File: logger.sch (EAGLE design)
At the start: 55 parts, among them IC1 LTC4412, J1 POWER_JACKPTH, Q1 FDN360P, Q2 FDN360P, U1 FT232RL

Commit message: exposed interfaces, button update, board layout
(1) Exposed SPI, I2C, and UART interfaces
(2) Added 1K resistors to UART to allow switching away from the computer
(3) Updated the buttons to PTH (higher button: RESET), PTH DPDT b/c of
    availability (LOG NOW)
(4) Reworked the board layout to keep the same form factor while adding
    many new screw terminals (and keeping the 3.5 mm spacing)
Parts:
- removed H2: (no value), SparkFun:M04SCREW
- removed S2: Reset, SparkFun:TAC_SWITCHSND
- added JP6: (no value), SparkFun-Connectors:M04SCREW
- added RESET: Reset, SparkFun-Electromechanical:SWITCH-MOMENTARY-2PTH
- added RX_SW: 1Kohm, rcl:R-US_R0603
- added TX_SW: 1K, rcl:R-US_R0603
- COUT: device SmartPrj:C-EUC0603 -> rcl:C-EUC0603
- MANUAL_LOG: device awickert:TL3350'TL3350' -> switch-misc:PVA1
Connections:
- removed net CS-EXT: H3.6
- removed net D7: H1.6, MCU.PD7(AIN1)
- new net D7-CS-EXT: H3.4, MCU.PD7(AIN1)
- new net N$10: TX_SW.1, U1.RXD
- new net N$9: RX_SW.1, U1.TXD
- net +3V3: now also H1.2, H1.4, H3.7; no longer H2.2, H2.4
- net A6: now also H1.1; no longer H2.1
- net A7: now also H1.3; no longer H2.3
- net CLK: now also H3.3; no longer H3.5
- net D3-INT1: now also H1.5; no longer H1.1
- net D5_MANUAL_LOG: now also MANUAL_LOG2.S; no longer MANUAL_LOG.M1
- net D6: now also H1.8; no longer H1.5
- net DI: now also H3.1; no longer H3.3
- net DO: now also H3.2; no longer H3.4
- net GND: now also H1.6, H3.6, MANUAL_LOG1.P, MANUAL_LOG2.P, RESET.1; no longer H1.2, H1.4, H1.7, MANUAL_LOG.COM1, MANUAL_LOG.COM2, S2.1, S2.2
- net INT0: now also MANUAL_LOG1.S; no longer MANUAL_LOG.M2
- net RESET: now also RESET.2; no longer S2.3, S2.4
- net RX-I: now also JP6.1, RX_SW.2; no longer H3.1, U1.TXD
- net SCL: now also JP6.4; no longer H3.8
- net SDA: now also JP6.3; no longer H3.7
- net TX-O: now also JP6.2, TX_SW.2; no longer H3.2, U1.RXD
- net VCC: now also H1.7, H3.5; no longer H1.3, H1.8
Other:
- moved on the sheet: H1, H3

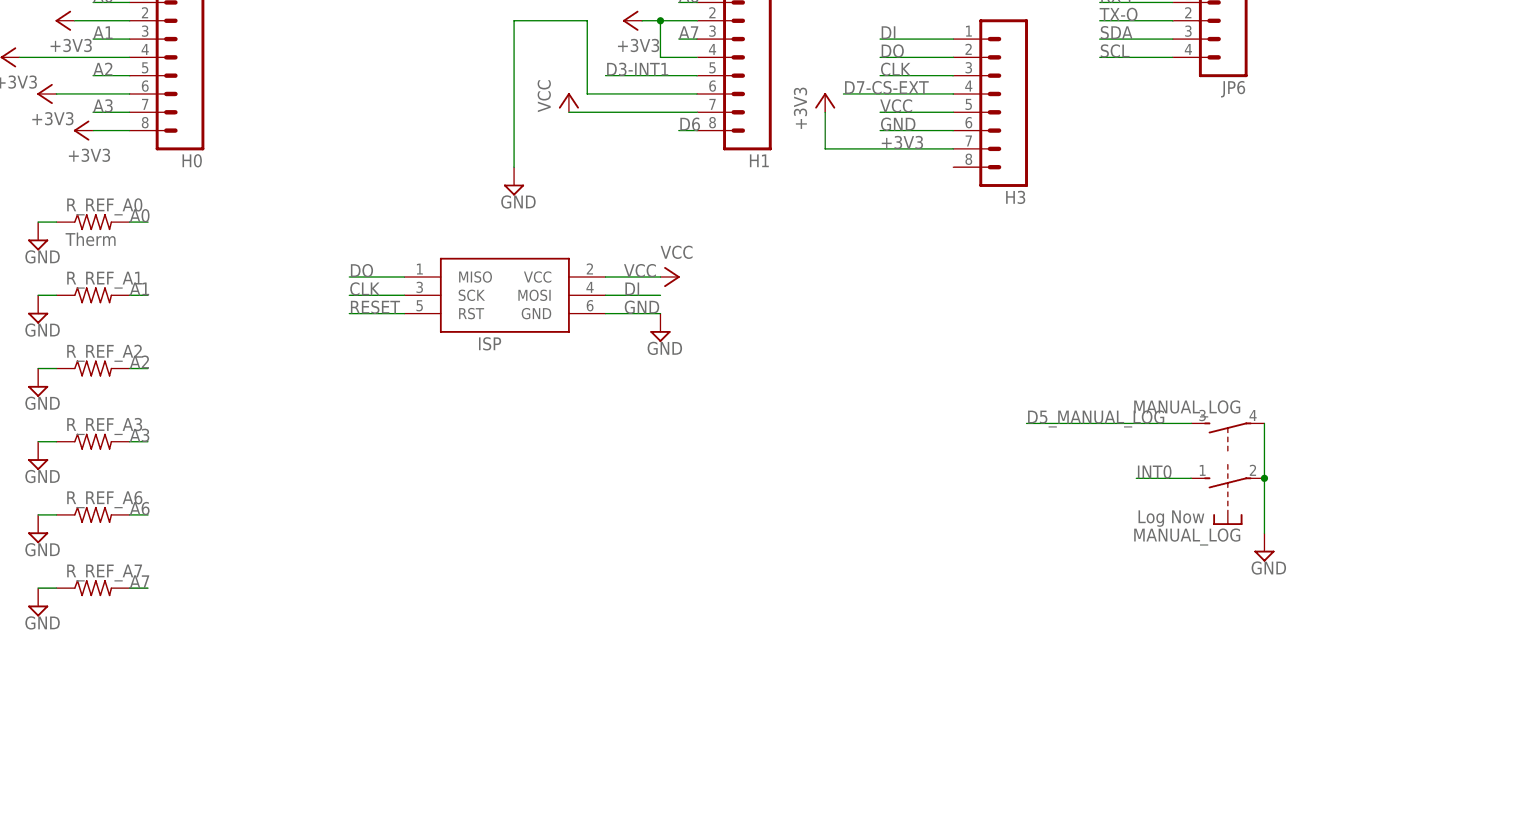
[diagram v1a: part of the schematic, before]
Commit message: 10nF chip caps for analog, following Gerhard Oberforcher
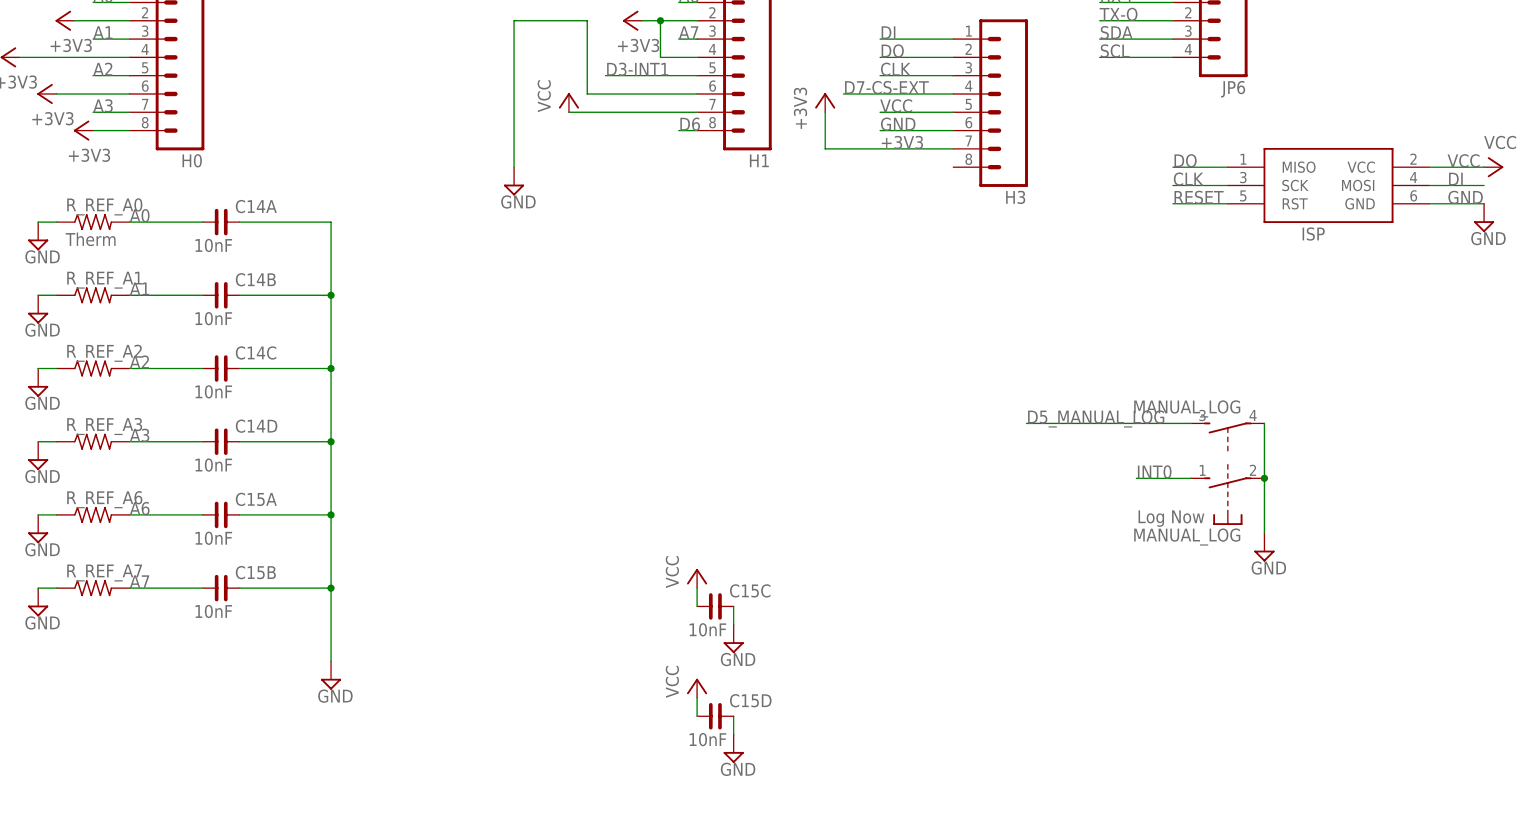
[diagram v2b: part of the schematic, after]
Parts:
- added C14, C15: 10nF, rc-master-smd:CCA_ECJ-0805
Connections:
- net A0: now also C14A.1
- net A1: now also C14B.1
- net A2: now also C14C.1
- net A3: now also C14D.1
- net A6: now also C15A.1
- net A7: now also C15B.1
- net GND: now also C14A.2, C14B.2, C14C.2, C14D.2, C15A.2, C15B.2, C15C.2, C15D.2
- net VCC: now also C15C.1, C15D.1
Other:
- moved on the sheet: ISP
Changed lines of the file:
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@@
 <clearance class="2" value="0.2032"/>
+</class>
+<class number="3" name="usbvcc" width="0.508" drill="0.508">
+<clearance class="3" value="0.1524"/>
+</class>
+<class number="4" name="aref" width="0.4064" drill="0">
 </class>
 </classes>
@@
 <part name="MANUAL_LOG" library="switch-misc" deviceset="PVA1" device="" value="Log Now"/>
 <part name="RESET" library="SparkFun-Electromechanical" deviceset="SWITCH-MOMENTARY-2" device="PTH" value="Reset"/>
+<part name="C14" library="rc-master-smd" deviceset="CCA_" device="ECJ-0805" value="10nF"/>
+<part name="C15" library="rc-master-smd" deviceset="CCA_" device="ECJ-0805" value="10nF"/>
+<part name="SUPPLY27" library="supply2" deviceset="GND" device=""/>
+<part name="SUPPLY37" library="supply2" deviceset="GND" device=""/>
+<part name="SUPPLY38" library="supply2" deviceset="GND" device=""/>
+<part name="P+17" library="supply1" deviceset="VCC" device=""/>
+<part name="P+22" library="supply1" deviceset="VCC" device=""/>
 </parts>
 <sheets>
@@
 <instance part="R_REF_A3" gate="G$1" x="208.28" y="58.42"/>
 <instance part="SUPPLY13" gate="GND" x="185.42" y="200.66"/>
-<instance part="ISP" gate="G$1" x="264.16" y="78.74"/>
-<instance part="P+11" gate="VCC" x="289.56" y="81.28" rot="R270"/>
-<instance part="SUPPLY14" gate="GND" x="287.02" y="73.66"/>
+<instance part="ISP" gate="G$1" x="378.46" y="93.98"/>
+<instance part="P+11" gate="VCC" x="403.86" y="96.52" rot="R270"/>
+<instance part="SUPPLY14" gate="GND" x="401.32" y="88.9"/>
 <instance part="PU1" gate="G$1" x="284.48" y="226.06" rot="R90"/>
 <instance part="PU2" gate="G$1" x="297.18" y="223.52" rot="R90"/>
@@
 <instance part="MANUAL_LOG" gate="2" x="365.76" y="60.96" rot="R90"/>
 <instance part="RESET" gate="G$1" x="88.9" y="149.86" rot="R90"/>
+<instance part="C14" gate="A" x="226.06" y="88.9"/>
+<instance part="C14" gate="B" x="226.06" y="78.74"/>
+<instance part="C14" gate="C" x="226.06" y="68.58"/>
+<instance part="C14" gate="D" x="226.06" y="58.42"/>
+<instance part="C15" gate="A" x="226.06" y="48.26"/>
+<instance part="C15" gate="B" x="226.06" y="38.1"/>
+<instance part="C15" gate="C" x="294.64" y="35.56"/>
+<instance part="C15" gate="D" x="294.64" y="20.32"/>
+<instance part="SUPPLY27" gate="GND" x="241.3" y="25.4"/>
+<instance part="SUPPLY37" gate="GND" x="297.18" y="15.24"/>
+<instance part="SUPPLY38" gate="GND" x="297.18" y="30.48"/>
+<instance part="P+17" gate="VCC" x="292.1" y="40.64"/>
+<instance part="P+22" gate="VCC" x="292.1" y="25.4"/>
 </instances>
 <busses>
@@
 </segment>
 <segment>
-<wire x1="279.4" y1="81.28" x2="287.02" y2="81.28" width="0.1524" layer="91"/>
-<label x="281.94" y="81.28" size="1.778" layer="95"/>
+<wire x1="393.7" y1="96.52" x2="401.32" y2="96.52" width="0.1524" layer="91"/>
+<label x="396.24" y="96.52" size="1.778" layer="95"/>
 <pinref part="ISP" gate="G$1" pin="VCC"/>
 <pinref part="P+11" gate="VCC" pin="VCC"/>
@@
 <pinref part="H3" gate="G$1" pin="5"/>
 </segment>
+<segment>
+<pinref part="C15" gate="C" pin="1"/>
+<wire x1="292.1" y1="35.56" x2="292.1" y2="38.1" width="0.1524" layer="91"/>
+<pinref part="P+17" gate="VCC" pin="VCC"/>
+</segment>
+<segment>
+<pinref part="C15" gate="D" pin="1"/>
+<wire x1="292.1" y1="20.32" x2="292.1" y2="22.86" width="0.1524" layer="91"/>
+<pinref part="P+22" gate="VCC" pin="VCC"/>
+</segment>
 </net>
 <net name="CS-SD" class="0">
@@
 </segment>
 <segment>
-<wire x1="279.4" y1="78.74" x2="287.02" y2="78.74" width="0.1524" layer="91"/>
-<label x="281.94" y="78.74" size="1.778" layer="95"/>
+<wire x1="393.7" y1="93.98" x2="401.32" y2="93.98" width="0.1524" layer="91"/>
+<label x="396.24" y="93.98" size="1.778" layer="95"/>
 <pinref part="ISP" gate="G$1" pin="MOSI"/>
 </segment>
@@
 </segment>
 <segment>
-<wire x1="251.46" y1="81.28" x2="243.84" y2="81.28" width="0.1524" layer="91"/>
-<label x="243.84" y="81.28" size="1.778" layer="95"/>
+<wire x1="365.76" y1="96.52" x2="358.14" y2="96.52" width="0.1524" layer="91"/>
+<label x="358.14" y="96.52" size="1.778" layer="95"/>
 <pinref part="ISP" gate="G$1" pin="MISO"/>
 </segment>
@@
 </segment>
 <segment>
-<wire x1="251.46" y1="78.74" x2="243.84" y2="78.74" width="0.1524" layer="91"/>
-<label x="243.84" y="78.74" size="1.778" layer="95"/>
+<wire x1="365.76" y1="93.98" x2="358.14" y2="93.98" width="0.1524" layer="91"/>
+<label x="358.14" y="93.98" size="1.778" layer="95"/>
 <pinref part="ISP" gate="G$1" pin="SCK"/>
 </segment>
@@
 </segment>
 <segment>
-<wire x1="279.4" y1="76.2" x2="287.02" y2="76.2" width="0.1524" layer="91"/>
-<label x="281.94" y="76.2" size="1.778" layer="95"/>
+<wire x1="393.7" y1="91.44" x2="401.32" y2="91.44" width="0.1524" layer="91"/>
+<label x="396.24" y="91.44" size="1.778" layer="95"/>
 <pinref part="ISP" gate="G$1" pin="GND"/>
 <pinref part="SUPPLY14" gate="GND" pin="GND"/>
@@
 <pinref part="MANUAL_LOG" gate="2" pin="P"/>
 </segment>
+<segment>
+<pinref part="C14" gate="A" pin="2"/>
+<wire x1="228.6" y1="88.9" x2="241.3" y2="88.9" width="0.1524" layer="91"/>
+<wire x1="241.3" y1="88.9" x2="241.3" y2="78.74" width="0.1524" layer="91"/>
+<wire x1="241.3" y1="78.74" x2="241.3" y2="68.58" width="0.1524" layer="91"/>
+<wire x1="241.3" y1="68.58" x2="241.3" y2="58.42" width="0.1524" layer="91"/>
+<pinref part="C14" gate="C" pin="2"/>
+<wire x1="241.3" y1="58.42" x2="241.3" y2="48.26" width="0.1524" layer="91"/>
+<wire x1="241.3" y1="48.26" x2="241.3" y2="38.1" width="0.1524" layer="91"/>
+<wire x1="241.3" y1="38.1" x2="241.3" y2="27.94" width="0.1524" layer="91"/>
+<wire x1="228.6" y1="68.58" x2="241.3" y2="68.58" width="0.1524" layer="91"/>
+<junction x="241.3" y="68.58"/>
+<pinref part="C14" gate="B" pin="2"/>
+<wire x1="228.6" y1="78.74" x2="241.3" y2="78.74" width="0.1524" layer="91"/>
+<junction x="241.3" y="78.74"/>
+<pinref part="C14" gate="D" pin="2"/>
+<wire x1="228.6" y1="58.42" x2="241.3" y2="58.42" width="0.1524" layer="91"/>
+<junction x="241.3" y="58.42"/>
+<pinref part="SUPPLY27" gate="GND" pin="GND"/>
+<pinref part="C15" gate="A" pin="2"/>
+<wire x1="228.6" y1="48.26" x2="241.3" y2="48.26" width="0.1524" layer="91"/>
+<junction x="241.3" y="48.26"/>
+<pinref part="C15" gate="B" pin="2"/>
+<wire x1="228.6" y1="38.1" x2="241.3" y2="38.1" width="0.1524" layer="91"/>
+<junction x="241.3" y="38.1"/>
+</segment>
+<segment>
+<pinref part="C15" gate="D" pin="2"/>
+<pinref part="SUPPLY37" gate="GND" pin="GND"/>
+<wire x1="297.18" y1="17.78" x2="297.18" y2="20.32" width="0.1524" layer="91"/>
+</segment>
+<segment>
+<pinref part="C15" gate="C" pin="2"/>
+<wire x1="297.18" y1="35.56" x2="297.18" y2="33.02" width="0.1524" layer="91"/>
+<pinref part="SUPPLY38" gate="GND" pin="GND"/>
+</segment>
 </net>
 <net name="TX-O" class="0">
@@
 </segment>
 <segment>
-<wire x1="243.84" y1="76.2" x2="251.46" y2="76.2" width="0.1524" layer="91"/>
-<label x="243.84" y="76.2" size="1.778" layer="95"/>
+<wire x1="358.14" y1="91.44" x2="365.76" y2="91.44" width="0.1524" layer="91"/>
+<label x="358.14" y="91.44" size="1.778" layer="95"/>
 <pinref part="ISP" gate="G$1" pin="RST"/>
 </segment>
@@
 </segment>
 <segment>
-<wire x1="213.36" y1="68.58" x2="215.9" y2="68.58" width="0.1524" layer="91"/>
+<wire x1="213.36" y1="68.58" x2="223.52" y2="68.58" width="0.1524" layer="91"/>
 <label x="213.36" y="68.58" size="1.778" layer="95"/>
 <pinref part="R_REF_A2" gate="G$1" pin="2"/>
+<pinref part="C14" gate="C" pin="1"/>
 </segment>
 <segment>
@@
 </segment>
 <segment>
-<wire x1="213.36" y1="88.9" x2="215.9" y2="88.9" width="0.1524" layer="91"/>
+<wire x1="213.36" y1="88.9" x2="223.52" y2="88.9" width="0.1524" layer="91"/>
 <label x="213.36" y="88.9" size="1.778" layer="95"/>
 <pinref part="R_REF_A0" gate="G$1" pin="2"/>
+<pinref part="C14" gate="A" pin="1"/>
 </segment>
 </net>
@@
 </segment>
 <segment>
-<wire x1="213.36" y1="58.42" x2="215.9" y2="58.42" width="0.1524" layer="91"/>
+<wire x1="213.36" y1="58.42" x2="223.52" y2="58.42" width="0.1524" layer="91"/>
 <label x="213.36" y="58.42" size="1.778" layer="95"/>
 <pinref part="R_REF_A3" gate="G$1" pin="2"/>
+<pinref part="C14" gate="D" pin="1"/>
 </segment>
 <segment>
@@
 </segment>
 <segment>
-<wire x1="213.36" y1="48.26" x2="215.9" y2="48.26" width="0.1524" layer="91"/>
+<wire x1="213.36" y1="48.26" x2="223.52" y2="48.26" width="0.1524" layer="91"/>
 <label x="213.36" y="48.26" size="1.778" layer="95"/>
 <pinref part="R_REF_A6" gate="G$1" pin="2"/>
+<pinref part="C15" gate="A" pin="1"/>
 </segment>
 </net>
@@
 </segment>
 <segment>
-<wire x1="213.36" y1="38.1" x2="215.9" y2="38.1" width="0.1524" layer="91"/>
+<wire x1="213.36" y1="38.1" x2="223.52" y2="38.1" width="0.1524" layer="91"/>
 <label x="213.36" y="38.1" size="1.778" layer="95"/>
 <pinref part="R_REF_A7" gate="G$1" pin="2"/>
+<pinref part="C15" gate="B" pin="1"/>
 </segment>
 </net>
@@
 </segment>
 <segment>
-<wire x1="213.36" y1="78.74" x2="215.9" y2="78.74" width="0.1524" layer="91"/>
+<wire x1="213.36" y1="78.74" x2="223.52" y2="78.74" width="0.1524" layer="91"/>
 <label x="213.36" y="78.74" size="1.778" layer="95"/>
 <pinref part="R_REF_A1" gate="G$1" pin="2"/>
-</segment>
-</net>
+<pinref part="C14" gate="B" pin="1"/>
+</segment>
+</net>

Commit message: a big mess of getting a new FTDI chip
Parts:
- added C1, C10, C11, C12, C13, C16, C4, C5, C8, C9: 100n, rcl:C-EU
- added C17, C20: 0.1uF, SparkFun-Capacitors:CAP0402-CAP
- added C18, C19: 47pF, SparkFun-Capacitors:CAP0402-CAP
- added C2, C3, C6, C7: 22p, rcl:C-EU
- added C21: 10uF, SparkFun-Passives:CAP_POL1206
- added F1, F2: 500mA, rcl:L-EUL1812
- added IC2, IC4: ATMEGA8, atmel:AT90S4433P
- added IC3, IC5: FT232RL, SmartPrj:FT232RL
- added J2, J3, J5, J6: (no value), pinhead:PINHD-1X8
- added J4, J7: (no value), pinhead:PINHD-1X6
- added JP7, JP8: USB-B, SparkFun-Connectors:USBPTH
- added LED1: RED, SparkFun-LED:LED0603
- added LED2: YELLOW, SparkFun-LED:LED0603
- added Q3, Q4: 16MHz, crystal:CRYTALHC49S
- added Q5: 2N7002PW, SparkFun-DiscreteSemi:MOSFET-NCHANNELSOT323
- added R1, R3, R4, R5, R6, R7, R8, R9: 1k, rcl:R-EU_
- added R10, R2: 100_NM, rcl:R-EU_
- added R11, R12: 27, SparkFun-Resistors:RESISTOR0402-RES
- added R13, R14: 1k, SparkFun-Passives:RESISTOR0402-RES
- added R15, R16: 10k, SparkFun-Passives:RESISTOR0402-RES
- added RX1, RX2, TX1, TX2: (no value), led:LED0805ROUND
- added SJ1: (no value), SparkFun-Passives:SOLDERJUMPER_2WAYS
- added SJ2: TXLED, SparkFun-Passives:SOLDERJUMPERTRACE
- added SJ3: RXLED, SparkFun-Passives:SOLDERJUMPERTRACE
- added U2: FT232RLSSOP, SparkFun-DigitalIC:FT232RLSSOP
- added U3: FT231XS, SparkFun-DigitalIC:FT231XS
- added USBD2, USBD4: 0.1uF, resistor:C-EUC0603
- added USBD3, USBD5: 10uF, SparkFun:CAP_POL1206
- added X1, X3: (no value), jumper:JP4E
- added X2, X4: (no value), SmartPrj:PN61729
- added X5: USB-MICROB, SparkFun-Connectors:USB-MICROB
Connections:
- new net +5V: C1.1, C10.1, C12.1, C5.1, IC2.AVCC, IC2.VCC, IC3.RESET#, IC3.VCC5I, IC3.VCCIO, IC4.AVCC, IC4.VCC, IC5.RESET#, IC5.VCC5I, IC5.VCCIO, R1.2, R3.2, R4.2, R5.2
- new net 3.3V: LED1.A, LED2.A, Q5.G, R15.2, SJ1.1
- new net AREF: IC2.AREF, IC4.AREF
- new net CBUS0: U3.CBUS0
- new net CBUS3: U3.CBUS3
- new net CTS: IC3.CTS#, IC5.CTS#, U3.!CTS, X1.1, X3.1
- new net D+: IC3.USBDP, IC5.USBDP, X2.3, X4.3
- new net D-: IC3.USBDM, IC5.USBDM, X2.2, X4.2
- new net DCD: IC3.DCD#, IC5.DCD#, U3.!DCD, X1.3, X3.3
- new net DSR: IC3.DSR#, IC5.DSR#, U3.!DSR, X1.2, X3.2
- new net M8RXD: IC3.TXD, IC5.TXD, R6.2, R8.2
- new net M8TXD: IC3.RXD, IC5.RXD, R7.2, R9.2
- new net MISO: IC2.(MISO)PB4, IC4.(MISO)PB4, J3.5, J6.5
- new net MOSI: IC2.(MOSI)PB3, IC4.(MOSI)PB3, J3.4, J6.4
- new net N$11: C2.2, IC2.XTAL1, Q3.1
- new net N$12: C3.2, IC2.XTAL2, Q3.2
- new net N$13: IC2.(INT0)PD2, J2.3
- new net N$14: IC2.(INT1)PD3, J2.4
- new net N$15: IC2.(T0)PD4, J2.5
- new net N$16: IC2.(T1)PD5, J2.6
- new net N$17: IC2.(AIN0)PD6, J2.7
- new net N$18: IC2.(AIN1)PD7, J2.8
- new net N$19: IC2.(ADC0)PC0), J4.1
- new net N$20: IC2.(ADC1)PC1, J4.2
- new net N$21: IC2.(ADC2)PC2, J4.3
- new net N$22: IC2.(ADC3)PC3, J4.4
- new net N$23: IC2.(ADC4)PC4, J4.5
- new net N$24: IC2.(ADC5)PC5, J4.6
- new net N$25: IC2.(ICP)PB0, J3.1
- new net N$26: IC2.(OC1)PB1, J3.2
- new net N$27: C6.2, IC4.XTAL1, Q4.1
- new net N$28: F1.2, X4.1
- new net N$29: C7.2, IC4.XTAL2, Q4.2
- new net N$30: IC4.(INT0)PD2, J5.3
- new net N$31: IC4.(INT1)PD3, J5.4
- new net N$32: IC3.GPIO1, RX1.C
- new net N$33: IC4.(T0)PD4, J5.5
- new net N$34: IC3.GPIO0, TX1.C
- new net N$35: R4.1, RX1.A
- new net N$36: R5.1, TX1.A
- new net N$37: IC4.(T1)PD5, J5.6
- new net N$38: IC4.(AIN0)PD6, J5.7
- new net N$39: IC4.(AIN1)PD7, J5.8
- new net N$40: IC4.(ADC0)PC0), J7.1
- new net N$41: IC4.(ADC1)PC1, J7.2
- new net N$42: IC4.(ADC2)PC2, J7.3
- new net N$43: IC4.(ADC3)PC3, J7.4
- new net N$44: IC4.(ADC4)PC4, J7.5
- new net N$45: IC4.(ADC5)PC5, J7.6
- new net N$46: IC4.(ICP)PB0, J6.1
- new net N$47: IC4.(OC1)PB1, J6.2
- new net N$48: IC5.GPIO1, RX2.C
- new net N$49: IC5.GPIO0, TX2.C
- new net N$50: R1.1, RX2.A
- new net N$51: R3.1, TX2.A
- new net N$52: F2.2, X2.1
- new net N$53: IC5.AGND, IC5.GND1, IC5.GND2, IC5.GND3, IC5.TEST
- new net N$54: JP7.D+, U2.USBDP
- new net N$55: JP7.D-, U2.USBDM
- new net N$56: R11.2, U3.USBDM
- new net N$57: R12.1, U3.USBDP
- new net N$58: C18.1, R12.2, X5.D+
- new net N$59: C19.1, R11.1, X5.D-
- new net N$60: LED2.C, R13.2
- new net N$61: LED1.C, R14.2
- new net N$62: R13.1, SJ2.2
- new net N$63: R14.1, SJ3.2
- new net N$64: JP8.D+
- new net N$65: JP8.D-
- new net PD0: IC2.(RXD)PD0, J2.1, R8.1
- new net PD1: IC2.(TXD)PD1, J2.2, R9.1
- new net PD2: IC4.(RXD)PD0, J5.1, R6.1
- new net PD3: IC4.(TXD)PD1, J5.2, R7.1
- new net RI: IC3.RI#, IC5.RI#, U3.!RI, X1.4, X3.4
- new net RTS: IC3.RTS#, IC5.RTS#, R10.1, R2.1, U3.!RTS
- new net RXD: U3.RXD
- new net RXLED: SJ3.1, U3.CBUS1
- new net SCK: IC2.(SCK)PB5, IC4.(SCK)PB5, J3.6, J6.6
- new net SS: IC2.(SS)PB2, IC4.(SS)PB2, J3.3, J6.3
- new net TXD: U3.TXD
- new net TXLED: SJ2.1, U3.CBUS2
- new net USBVCC: C4.1, C9.1, F1.1, F2.1
- new net VCC3O: C11.2, C8.2, IC3.VCC30, IC5.VCC30
- new net VOUT: R16.2, SJ1.2
- net DTR: now also C13.1, C16.1, IC3.DTR#, IC5.DTR#, Q5.S, R15.1, U3.!DTR
- net GND: now also C1.2, C10.2, C11.1, C12.2, C17.2, C18.2, C19.2, C2.1, C20.2, C21.-, C3.1, C4.2, C5.2, C6.1, C7.1, C8.1, C9.2, IC2.AGND, IC2.GND, IC3.AGND, IC3.GND1, IC3.GND2, IC3.GND3, IC3.TEST, IC4.AGND, IC4.GND, JP7.GND, JP8.GND, U2.AGND, U2.GND18, U2.GND21, U2.GND7, U2.TEST, U3.GND@16, U3.GND@6, USBD2.2, USBD3.-, USBD4.2, USBD5.-, X2.4, X2.P$1, X2.P$2, X4.4, X4.P$1, X4.P$2, X5.GND
- net RESET: now also C13.2, C16.2, IC2.RESET, IC4.RESET, Q5.D, R10.2, R16.1, R2.2
- net VCC: now also C17.1, C21.+, SJ1.3, X5.VBUS
- net VUSB: now also C20.1, JP7.VBUS, JP8.VBUS, U2.VCC, U2.VCCIO, U3.!RESET, U3.VCC, U3.VCCIO, USBD2.1, USBD3.+, USBD4.1, USBD5.+
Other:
- note added: "0"
- note added: "1"
- note added: "10"
- note added: "11"
- note added: "12"
- note added: "13"
- note added: "2"
- note added: "3"
- note added: "4"
- note added: "5"
- note added: "6"
- note added: "7"
- note added: "8"
- note added: "9"
- note added: "Arduino 2009"
